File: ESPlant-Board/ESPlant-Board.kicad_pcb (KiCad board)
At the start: 2 copper layers, 22 x 123.7 mm, 37 parts, among them J1 Conn_01x05, U1 HC-TYPE-C-16P-01A-G, U13 ESP32-C6-MINI-1/U, U3 Reset, U4 Boot, U5 Temp/Humid-Sensor, U6 Light sensor, U7 AMS1117-3_3, U8 MK-12C02-G025

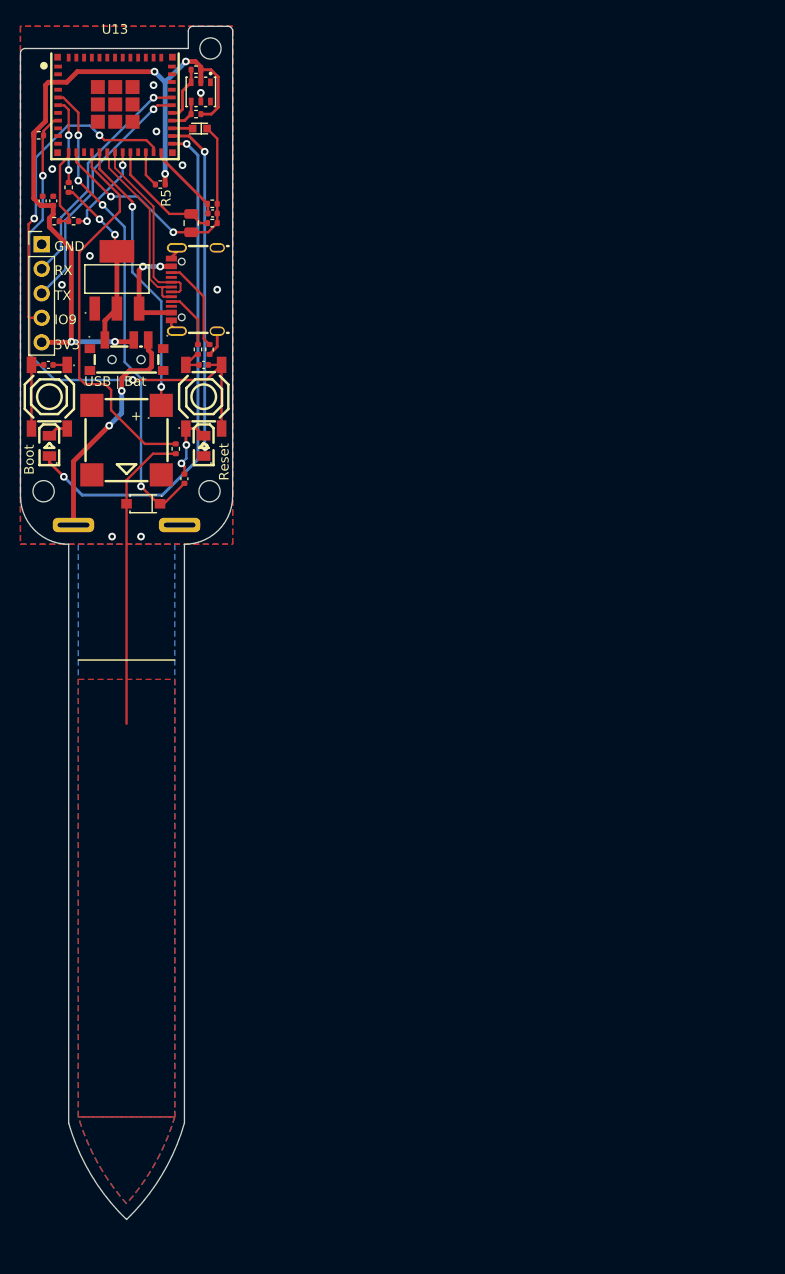
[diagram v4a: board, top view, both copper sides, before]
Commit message: Board: Make ESPlant-Board 4 layer (wip)
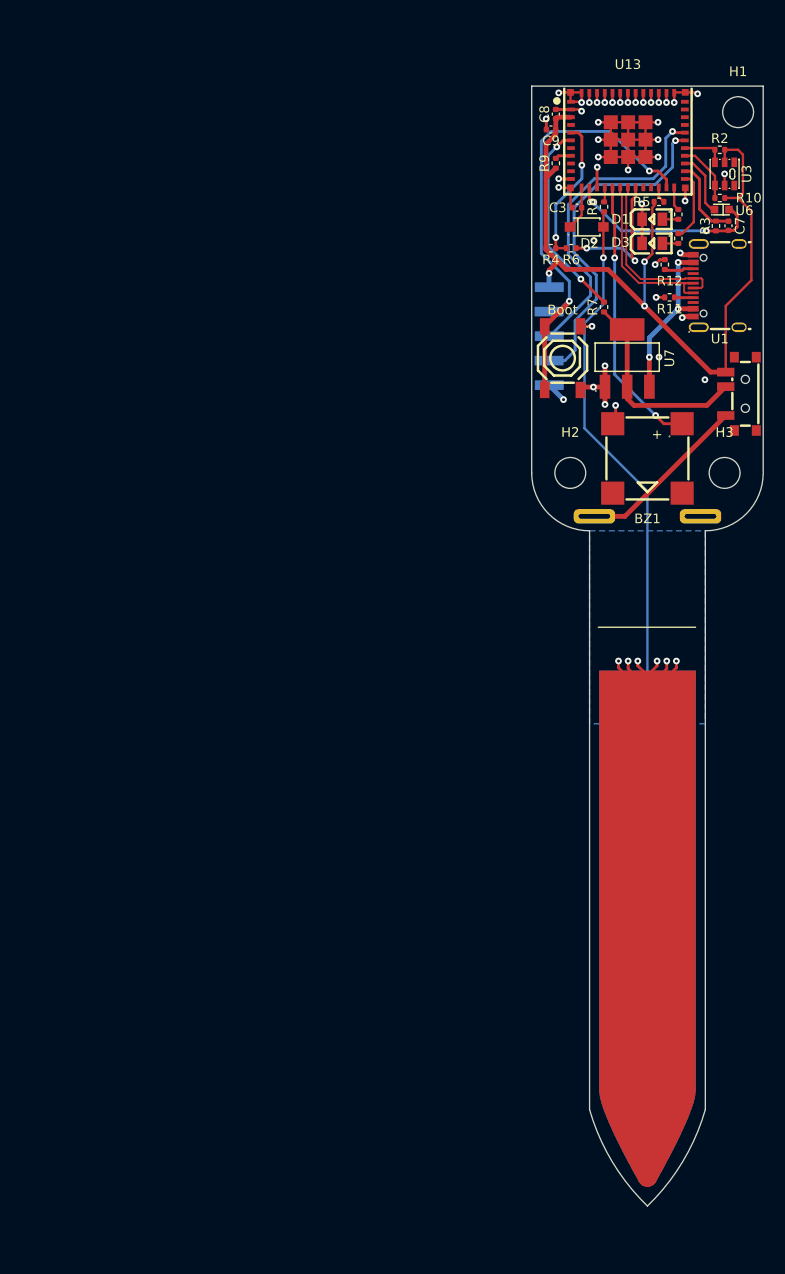
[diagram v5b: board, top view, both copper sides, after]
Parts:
- removed C1, C2, C5: 100nF, Capacitor_SMD:C_0402_1005Metric
- removed R1: 10M, Resistor_SMD:R_0402_1005Metric
- removed U4: Boot, CustomFootprints:SW-SMD_4P-L5.1-W5.1-P3.70-LS6.5-TL-2
- removed U5: Temp/Humid-Sensor, CustomFootprints:SENSOR-SMD_L3.0-W3.0-P1.00-BR
- added Boot: Button, CustomFootprints:SW-SMD_4P-L5.1-W5.1-P3.70-LS6.5-TL-2, F.Cu at (156.2, 132.1)
- added C4: 7pF-27pF, A=2.75cm^2, CustomFootprints:Sensor-Tip, B.Cu at (165.0, 165.0)
- added H1: MountingHole, MountingHole:MountingHole_3.2mm_M3, F.Cu at (174.4, 106.6)
- added H2: MountingHole, MountingHole:MountingHole_3.2mm_M3, F.Cu at (157.0, 144.0)
- added H3: MountingHole, MountingHole:MountingHole_3.2mm_M3, F.Cu at (173.0, 144.0)
- added R13: 120, Resistor_SMD:R_0402_1005Metric, F.Cu at (168.2, 117.2)
- added R14: 120, Resistor_SMD:R_0402_1005Metric, F.Cu at (168.2, 119.7)
- C7: value 47uF -> 10uF; footprint Capacitor_SMD:C_0805_2012Metric -> Capacitor_SMD:C_0402_1005Metric
- J1: footprint Connector_PinHeader_2.54mm:PinHeader_1x05_P2.54mm_Vertical -> CustomFootprints:PinHeader_1x05_P2.54mm_Vertical_SMD; moved to B.Cu
- R3: value 1k -> 47k
- U3: value Reset -> AHT20-F; footprint CustomFootprints:SW-SMD_4P-L5.1-W5.1-P3.70-LS6.5-TL-2 -> CustomFootprints:SENSOR-SMD-6_AHT20
- moved D1 66.8 mm to (165.5, 117.7), turned to 0 degrees
- moved U8 63.8 mm to (174.7, 135.8), turned to 90 degrees
- moved U3 58.7 mm to (173.0, 113.0), turned to -90 degrees
- moved R7 56.9 mm to (160.5, 126.8)
- moved C7 55.7 mm to (173.4, 118.4)
- moved R10 55.0 mm to (172.5, 115.5)
- moved R2 54.9 mm to (172.5, 110.5)
- moved U6 54.7 mm to (172.7, 116.7)
- moved J1 54.7 mm to (156.1, 129.8)
- moved D2 54.2 mm to (158.7, 118.5), turned to 0 degrees
- moved U1 54.1 mm to (172.1, 124.6)
- moved BZ1 54.0 mm to (165.0, 142.5)
- moved U9 54.0 mm to (165.0, 148.5)
- moved R9 53.7 mm to (155.5, 111.9), turned to 90 degrees
- moved U7 53.5 mm to (162.9, 132.1)
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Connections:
- C7 pad 2: /Light_Sensor_Select_2 -> /Light_Sensor_Select
- D1 pad 1: /LED_GREEN -> Net-(D1-A)
- D3 pad 1: /LED_RED -> Net-(D3-+)
- J1 pad 2: /TX -> /RX
- J1 pad 3: /RX -> /TX
- R3 pad 2: /Light_Sensor_Select_2 -> /Light_Sensor_Select
- U1 pad 1: GND -> unconnected-(U1-SHELL-Pad1)
- U1 pad 2: GND -> unconnected-(U1-SHELL-Pad2)
- U1 pad 3: GND -> unconnected-(U1-SHELL-Pad3)
- U1 pad 4: GND -> unconnected-(U1-SHELL-Pad4)
- U13 pad 12: /Voltage_Measurement_Analog -> /AD_Capacitance
- U13 pad 20: /Light_Sensor_Select_2 -> unconnected-(U13-IO15-Pad20)
- U13 pad 24: /Light_Sensor_Select_1 -> /LED_GREEN
- U13 pad 25: /LED_GREEN -> /LED_RED
- U13 pad 26: /LED_RED -> /Light_Sensor_Select
- U13 pad 5: /AD_Capacitance -> /Voltage_Measurement_Analog
- U3 pad 1: GND -> unconnected-(U3-NC-Pad1)
- U3 pad 2: /EN -> +3V3
- U8 pad 1: /USB -> /BAT
- U8 pad 2: +3V3 -> /USB
- U8 pad 3: /BAT -> +3V3
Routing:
- net GND: track 19.9 -> 103.0 mm, vias 12 -> 49
- net /EN: track 55.4 -> 1.68 mm, vias 2 -> 0
- net /LED_GREEN: track 53.7 -> 2.47 mm, vias 2 -> 0
- net /AD_Capacitance: track 50.3 -> 4.61 mm, vias 4 -> 0
- net /Square_Wave_Signal: track 40.4 -> 1.53 mm
- net /LED_RED: track 35.7 -> 7.27 mm, vias 2 -> 0
- net /SensorCapV: track 31.5 -> 51.6 mm, vias 0 -> 1
- net /Light_Sensor_Select_2: track 12.4 -> 0.00 mm
- net Net-(U13-IO3): track 8.83 -> 20.6 mm
- net /RX: track 26.0 -> 35.6 mm
- net /TX: track 24.4 -> 33.4 mm
- net /Light_Sensor_Analog: track 29.2 -> 20.3 mm
- net /Light_Sensor_Select: track 0.00 -> 8.48 mm
- net /Light_Sensor_Select_1: track 8.35 -> 0.00 mm
- net +3V3: track 77.3 -> 84.4 mm, vias 5 -> 3
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- added copper zone on In1.Cu, net GND
- added copper zone on In2.Cu, net GND
- removed copper zone on F.Cu, net /SensorCapV
- removed copper zone on F.Cu, net GND
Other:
- board size 22 x 123.7 mm -> 24 x 46.1 mm
- copper layers 2 -> 4
- board text removed: "3V3"
- board text removed: "Boot"
- board text removed: "ESPlant-v2.1"
- board text removed: "GND"
- board text removed: "IO9"
- board text removed: "M2"
- board text removed: "RX"
- board text removed: "Reset"
- board text removed: "TX"
- board text removed: "USB | Bat"

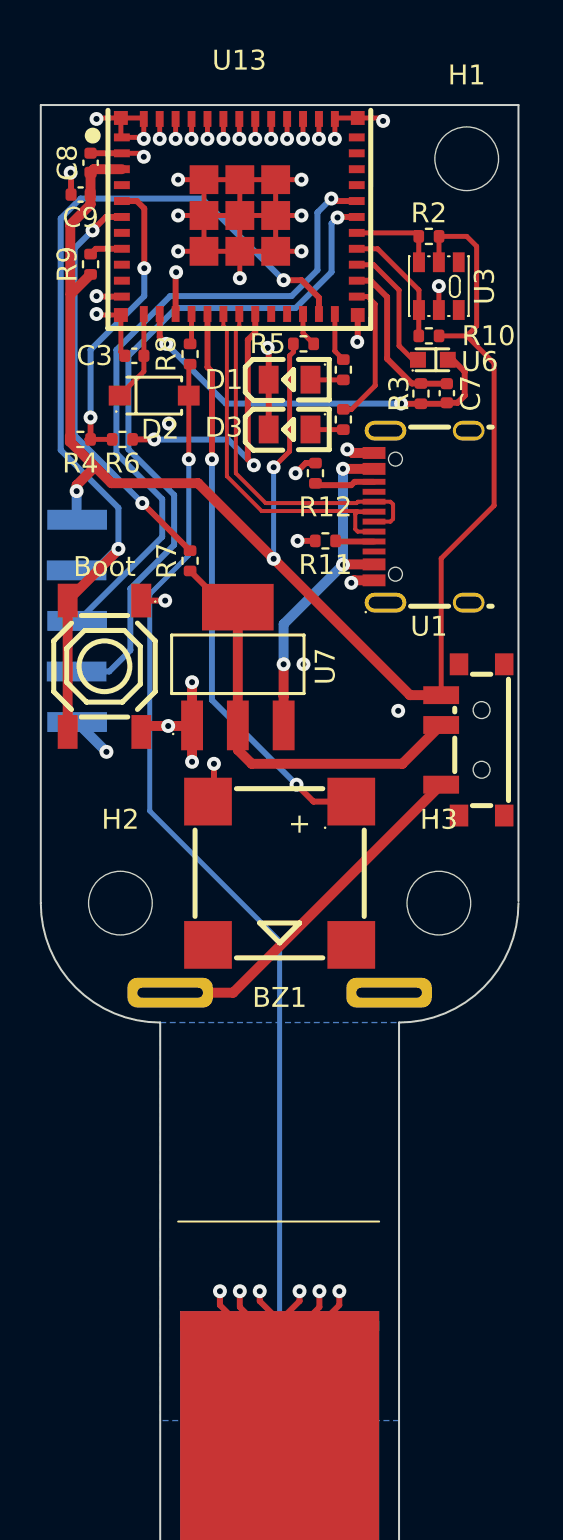
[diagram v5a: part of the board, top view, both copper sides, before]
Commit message: Board: Change from 2-layer to 4-layer board
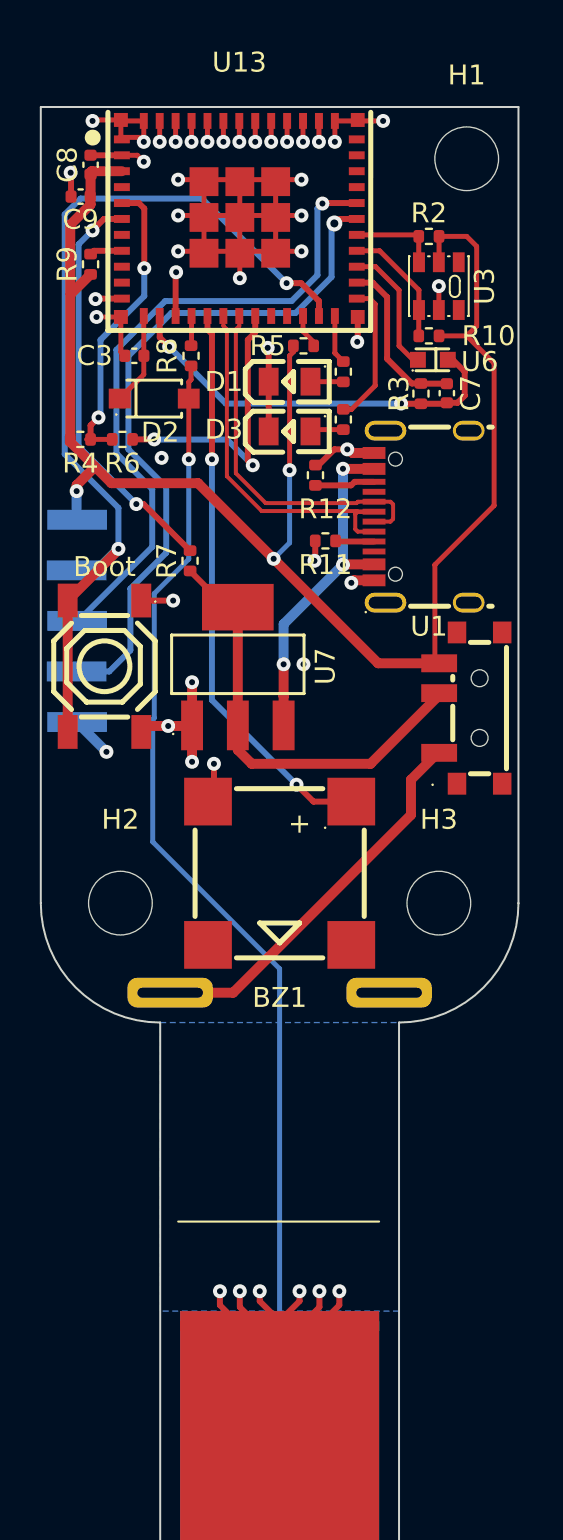
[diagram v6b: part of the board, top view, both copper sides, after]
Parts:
- moved U11 55.7 mm to (177.0, 112.8)
- moved U2 55.1 mm to (177.1, 140.8)
- moved U12 53.7 mm to (153.0, 112.8)
- moved U10 53.0 mm to (153.0, 140.8)
- moved U8 1.60 mm to (174.6, 134.2)
- moved D2 0.15 mm to (158.7, 118.7)
- moved R8 0.10 mm to (160.6, 116.5)
- moved C8 0.10 mm to (155.5, 106.9)
- moved U13 0.10 mm to (163.0, 109.6)
- moved C9 0.10 mm to (155.0, 108.5)
- moved D1 0.10 mm to (165.5, 117.8)
- moved D3 0.10 mm to (165.5, 120.3)
- moved R12 0.10 mm to (166.8, 122.5)
- moved R13 0.10 mm to (168.2, 117.3)
- moved R5 0.10 mm to (166.2, 116.0)
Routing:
- net GND: track 103.0 -> 106.0 mm, vias 49 -> 47
- net +3V3: track 84.4 -> 82.2 mm
- net /BAT: track 17.9 -> 19.5 mm
- net /USB: track 21.6 -> 22.3 mm
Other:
- board size 24 x 46.1 mm -> 24 x 46 mm

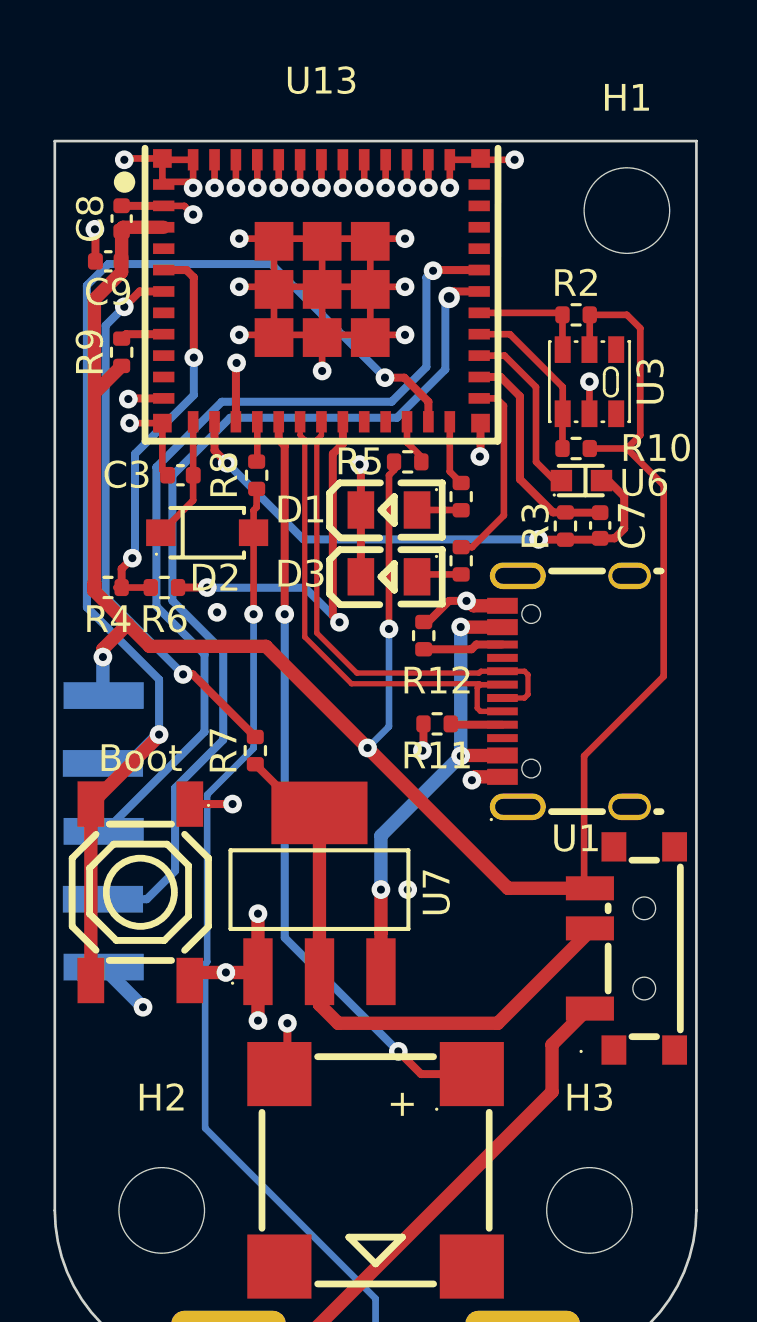
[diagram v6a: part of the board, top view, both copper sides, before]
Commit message: Panel: Add panelization script
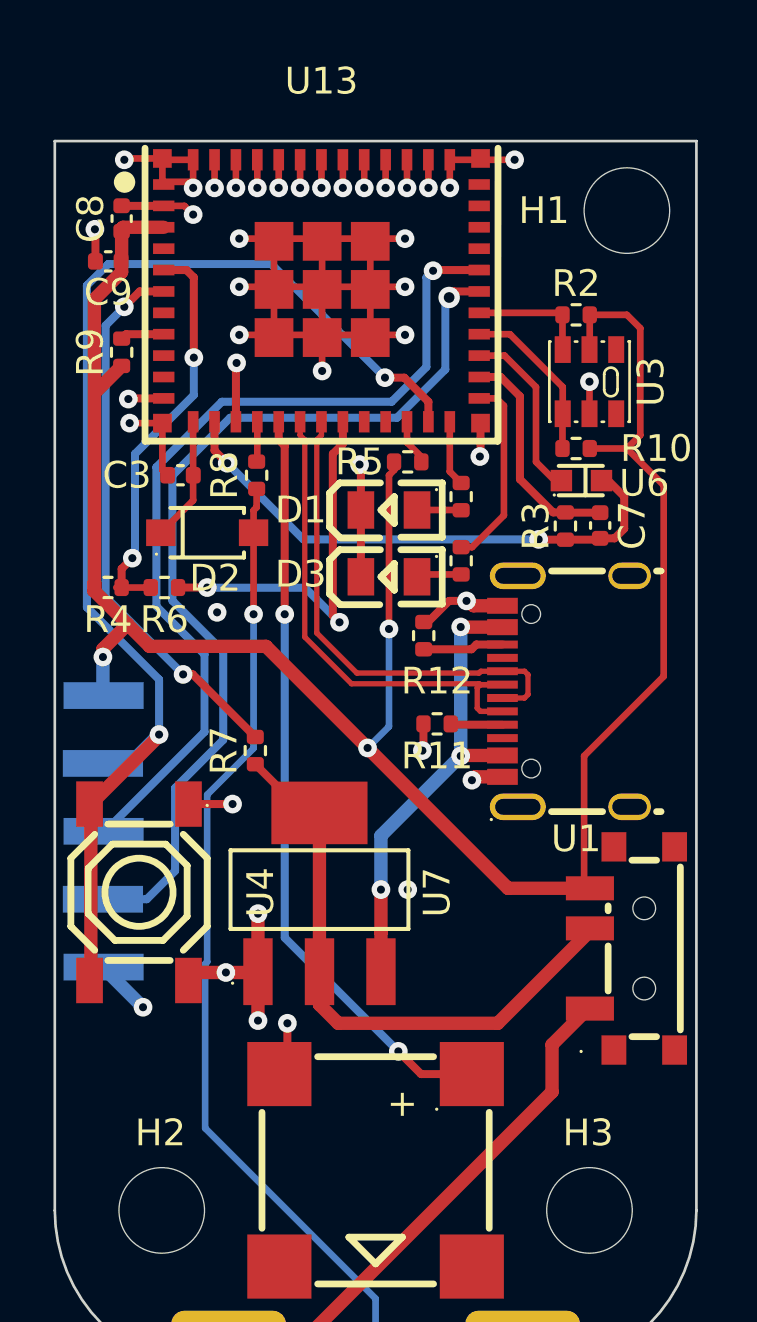
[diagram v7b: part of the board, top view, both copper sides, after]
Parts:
- removed Boot: Button, CustomFootprints:SW-SMD_4P-L5.1-W5.1-P3.70-LS6.5-TL-2
- added U4: Button, CustomFootprints:SW-SMD_4P-L5.1-W5.1-P3.70-LS6.5-TL-2, F.Cu at (156.1, 132.1)
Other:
- board text added: "Aconitum"
- board text added: "Blumy"

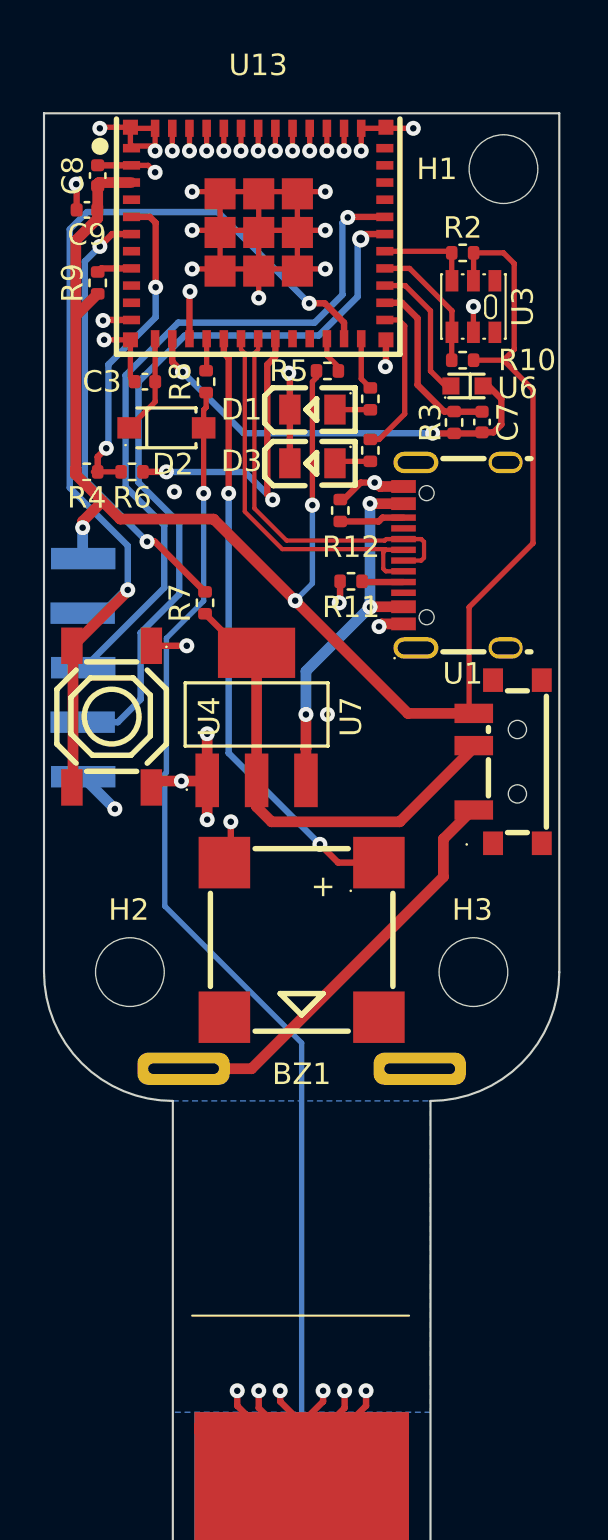
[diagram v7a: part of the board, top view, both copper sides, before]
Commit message: Update capacitor size
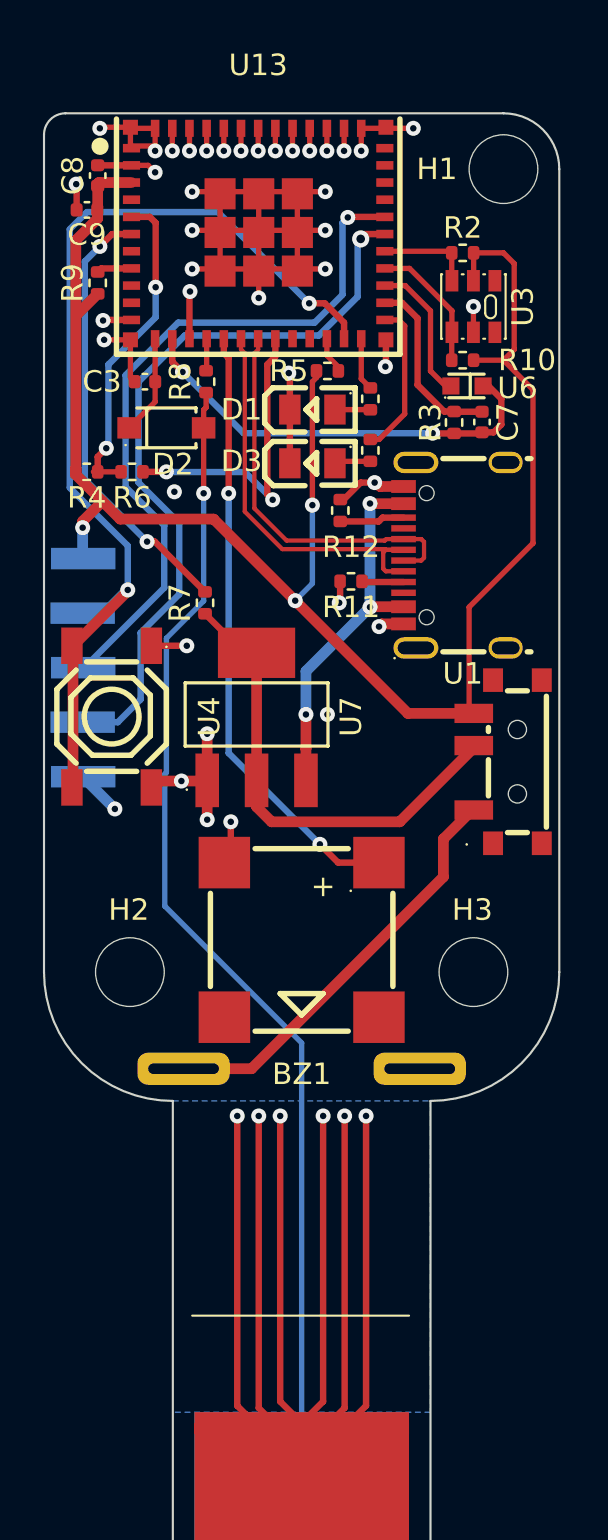
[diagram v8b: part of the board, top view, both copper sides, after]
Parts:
- C3: value 150pF -> 10nF
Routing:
- net GND: track 106.0 -> 182.8 mm
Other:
- outline, holes or cut-outs redrawn
